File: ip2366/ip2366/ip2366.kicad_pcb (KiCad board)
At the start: 4 copper layers, 60 parts, among them CN1 XT30PW-M, Q1 RU3030M2-VB, SW1 K2-1112SW-A4SW-04, U1 IP2366 (I2C VERSION)

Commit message: replace the inductor
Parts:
- L1: footprint easyeda2kicad:IND-SMD_2P-L16.9-W16.9 -> easyeda2kicad:IND-SMD_L13.5-W12.5
- moved L1 2.54 mm to (146.9, 83.2)
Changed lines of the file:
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@@
 		)
 	)
-	(footprint "easyeda2kicad:IND-SMD_2P-L16.9-W16.9"
-		(layer "F.Cu")
-		(at 146.55 85.75)
-		(property "Reference" "L1"
-			(at 0 -4 0)
-			(layer "F.SilkS")
-			(effects
-				(font
-					(size 1 1)
-					(thickness 0.15)
-				)
-			)
-		)
-		(property "Value" "10uH"
-			(at 0 4 0)
-			(layer "F.Fab")
-			(effects
-				(font
-					(size 1 1)
-					(thickness 0.15)
-				)
-			)
-		)
-		(property "Datasheet" ""
-			(at 0 0 0)
-			(layer "F.Fab")
-			(hide yes)
-			(effects
-				(font
-					(size 1.27 1.27)
-					(thickness 0.15)
-				)
-			)
-		)
-		(property "Description" ""
-			(at 0 0 0)
-			(layer "F.Fab")
-			(hide yes)
-			(effects
-				(font
-					(size 1.27 1.27)
-					(thickness 0.15)
-				)
-			)
-		)
-		(property "LCSC Part" "C2847588"
-			(at 0 0 0)
-			(unlocked yes)
-			(layer "F.Fab")
-			(hide yes)
-			(effects
-				(font
-					(size 1 1)
-					(thickness 0.15)
-				)
-			)
-		)
-		(sheetname "/")
-		(sheetfile "ip2366.kicad_sch")
-		(attr smd)
-		(fp_line
-			(start -8.83 -8.74)
-			(end -8.81 -6.49)
-			(stroke
-				(width 0.25)
-				(type solid)
-			)
-			(layer "F.SilkS")
-		)
-		(fp_line
-			(start -8.82 6.48)
-			(end -8.82 9.01)
-			(stroke
-				(width 0.25)
-				(type solid)
-			)
-			(layer "F.SilkS")
-		)
-		(fp_line
-			(start -8.82 9.01)
-			(end 8.96 8.92)
-			(stroke
-				(width 0.25)
-				(type solid)
-			)
-			(layer "F.SilkS")
-		)
-		(fp_line
-			(start 8.82 -8.77)
-			(end -8.83 -8.74)
-			(stroke
-				(width 0.25)
-				(type solid)
-			)
-			(layer "F.SilkS")
-		)
-		(fp_line
-			(start 8.84 -6.49)
-			(end 8.82 -8.77)
-			(stroke
-				(width 0.25)
-				(type solid)
-			)
-			(layer "F.SilkS")
-		)
-		(fp_line
-			(start 8.96 8.92)
-			(end 8.94 6.48)
-			(stroke
-				(width 0.25)
-				(type solid)
-			)
-			(layer "F.SilkS")
-		)
-		(fp_circle
-			(center -8.8 -8.45)
-			(end -8.77 -8.45)
-			(stroke
-				(width 0.06)
-				(type solid)
-			)
-			(fill no)
-			(layer "F.Fab")
-		)
-		(fp_text user "${REFERENCE}"
-			(at 0 0 0)
-			(layer "F.Fab")
-			(effects
-				(font
-					(size 1 1)
-					(thickness 0.15)
-				)
-			)
-		)
-		(pad "1" smd rect
-			(at -7.7 0)
-			(size 3.15 12.5)
-			(layers "F.Cu" "F.Mask" "F.Paste")
-			(net 6 "LX1")
-			(pinfunction "1")
-			(pintype "unspecified")
-		)
-		(pad "2" smd rect
-			(at 7.7 0)
-			(size 3.15 12.5)
-			(layers "F.Cu" "F.Mask" "F.Paste")
-			(net 9 "LX2")
-			(pinfunction "2")
-			(pintype "unspecified")
-		)
-		(embedded_fonts no)
-		(model "${EASYEDA2KICAD}/easyeda2kicad.3dshapes/IND-SMD_2P-L16.9-W16.9.wrl"
-			(offset
-				(xyz 0 -0 -0)
-			)
-			(scale
-				(xyz 1 1 1)
-			)
-			(rotate
-				(xyz 0 0 0)
-			)
-		)
-	)
 	(footprint "easyeda2kicad:C1210"
 		(layer "F.Cu")
@@
 			)
 		)
+	)
+	(footprint "easyeda2kicad:IND-SMD_L13.5-W12.5"
+		(layer "F.Cu")
+		(at 146.86 83.225)
+		(property "Reference" "L1"
+			(at 0 -4 0)
+			(layer "F.SilkS")
+			(effects
+				(font
+					(size 1 1)
+					(thickness 0.15)
+				)
+			)
+		)
+		(property "Value" "10uH"
+			(at 0 4 0)
+			(layer "F.Fab")
+			(effects
+				(font
+					(size 1 1)
+					(thickness 0.15)
+				)
+			)
+		)
+		(property "Datasheet" ""
+			(at 0 0 0)
+			(layer "F.Fab")
+			(hide yes)
+			(effects
+				(font
+					(size 1.27 1.27)
+					(thickness 0.15)
+				)
+			)
+		)
+		(property "Description" ""
+			(at 0 0 0)
+			(layer "F.Fab")
+			(hide yes)
+			(effects
+				(font
+					(size 1.27 1.27)
+					(thickness 0.15)
+				)
+			)
+		)
+		(property "LCSC Part" "C840531"
+			(at 0 0 0)
+			(unlocked yes)
+			(layer "F.Fab")
+			(hide yes)
+			(effects
+				(font
+					(size 1 1)
+					(thickness 0.15)
+				)
+			)
+		)
+		(sheetname "/")
+		(sheetfile "ip2366.kicad_sch")
+		(attr through_hole)
+		(fp_line
+			(start -6.86 -6.35)
+			(end 6.86 -6.35)
+			(stroke
+				(width 0.25)
+				(type solid)
+			)
+			(layer "F.SilkS")
+		)
+		(fp_line
+			(start -6.86 -2.98)
+			(end -6.86 -6.35)
+			(stroke
+				(width 0.25)
+				(type solid)
+			)
+			(layer "F.SilkS")
+		)
+		(fp_line
+			(start -6.86 6.35)
+			(end -6.86 3.05)
+			(stroke
+				(width 0.25)
+				(type solid)
+			)
+			(layer "F.SilkS")
+		)
+		(fp_line
+			(start 6.86 -6.35)
+			(end 6.86 -3.05)
+			(stroke
+				(width 0.25)
+				(type solid)
+			)
+			(layer "F.SilkS")
+		)
+		(fp_line
+			(start 6.86 2.98)
+			(end 6.86 6.35)
+			(stroke
+				(width 0.25)
+				(type solid)
+			)
+			(layer "F.SilkS")
+		)
+		(fp_line
+			(start 6.86 6.35)
+			(end -6.86 6.35)
+			(stroke
+				(width 0.25)
+				(type solid)
+			)
+			(layer "F.SilkS")
+		)
+		(fp_circle
+			(center -6.75 6.25)
+			(end -6.72 6.25)
+			(stroke
+				(width 0.06)
+				(type solid)
+			)
+			(fill no)
+			(layer "F.Fab")
+		)
+		(fp_text user "${REFERENCE}"
+			(at 0 0 0)
+			(layer "F.Fab")
+			(effects
+				(font
+					(size 1 1)
+					(thickness 0.15)
+				)
+			)
+		)
+		(pad "1" smd rect
+			(at -5.39 0)
+			(size 4.18 5.5)
+			(layers "F.Cu" "F.Mask" "F.Paste")
+			(net 6 "LX1")
+			(pinfunction "1")
+			(pintype "unspecified")
+		)
+		(pad "2" smd rect
+			(at 5.39 0)
+			(size 4.18 5.5)
+			(layers "F.Cu" "F.Mask" "F.Paste")
+			(net 9 "LX2")
+			(pinfunction "2")
+			(pintype "unspecified")
+		)
+		(embedded_fonts no)
+		(model "${EASYEDA2KICAD}/easyeda2kicad.3dshapes/IND-SMD_L13.5-W12.5.wrl"
+			(offset
+				(xyz 0 -0 0)
+			)
+			(scale
+				(xyz 1 1 1)
+			)
+			(rotate
+				(xyz 0 0 0)
+			)
+		)

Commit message: aktueller stand
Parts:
- added R21: 0R, Resistor_SMD:R_0603_1608Metric_Pad0.98x0.95mm_HandSolder, F.Cu at (146.3, 52.4)
- moved C22 48.1 mm to (159.6, 52.9)
- moved C23 47.6 mm to (165.4, 53.3)
- moved C20 47.4 mm to (156.2, 52.9)
- moved C19 46.7 mm to (152.8, 52.9)
- moved C2 45.4 mm to (119.5, 52.8)
- moved Q1 45.4 mm to (114.5, 59.2)
- moved C4 44.8 mm to (122.9, 52.8)
- moved C6 44.2 mm to (126.2, 52.8)
- moved R3 43.1 mm to (117.9, 60.7), turned to 180 degrees
- moved CN1 42.1 mm to (173.1, 63.0)
- moved C5 40.5 mm to (115.2, 64.8)
- moved SW1 39.8 mm to (101.7, 74.3)
- moved R20 39.4 mm to (105.6, 73.9), turned to 180 degrees
- moved R19 38.7 mm to (105.6, 72.3), turned to 180 degrees
- moved C7 38.5 mm to (109.8, 57.0), turned to 180 degrees
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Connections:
- Q1 pad 1: unconnected-(Q1-S-Pad1) -> VBUS
- Q1 pad 3: unconnected-(Q1-S-Pad3) -> VBUS
- RNTC1 pad 1: NTC -> Net-(R21-Pad2)
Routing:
- net +BATT: track 0.00 -> 126.0 mm, vias 0 -> 1
- net EN: track 0.00 -> 74.5 mm, vias 0 -> 2
- net CC2: track 0.00 -> 59.2 mm, vias 0 -> 2
- net DP: track 0.00 -> 58.0 mm, vias 0 -> 2
- net DM: track 0.00 -> 56.4 mm, vias 0 -> 2
- net CC1: track 0.00 -> 50.4 mm, vias 0 -> 2
- net VBUS: track 0.00 -> 38.4 mm, vias 0 -> 2
- net LED3: track 0.00 -> 37.8 mm, vias 0 -> 2
- net VBUS1: track 0.00 -> 37.5 mm
- net LED2: track 0.00 -> 37.2 mm, vias 0 -> 2
- net LED1: track 0.00 -> 35.9 mm, vias 0 -> 2
- net VSET: track 0.00 -> 29.1 mm, vias 0 -> 2
- net LG1: track 0.00 -> 27.3 mm, vias 0 -> 2
- net LG2: track 0.00 -> 27.2 mm, vias 0 -> 2
- net PSET: track 0.00 -> 25.9 mm, vias 0 -> 4
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- added copper zone on F.Cu, net +BATT
- added copper zone on F.Cu, net -BATT
- added copper zone on B.Cu, net GND
- added copper zone on F.Cu, net GND
- added copper zone on In1.Cu, net GND
- added copper zone on In2.Cu, net GND
- added copper zone on F.Cu, net LX1
- added copper zone on F.Cu, net LX2
- added copper zone on F.Cu, net VBUS
- added copper zone on F.Cu, net VBUS-
- added copper zone on F.Cu, net VBUS1
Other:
- board outline added: 80 x 32 mm
- board text added: "+"

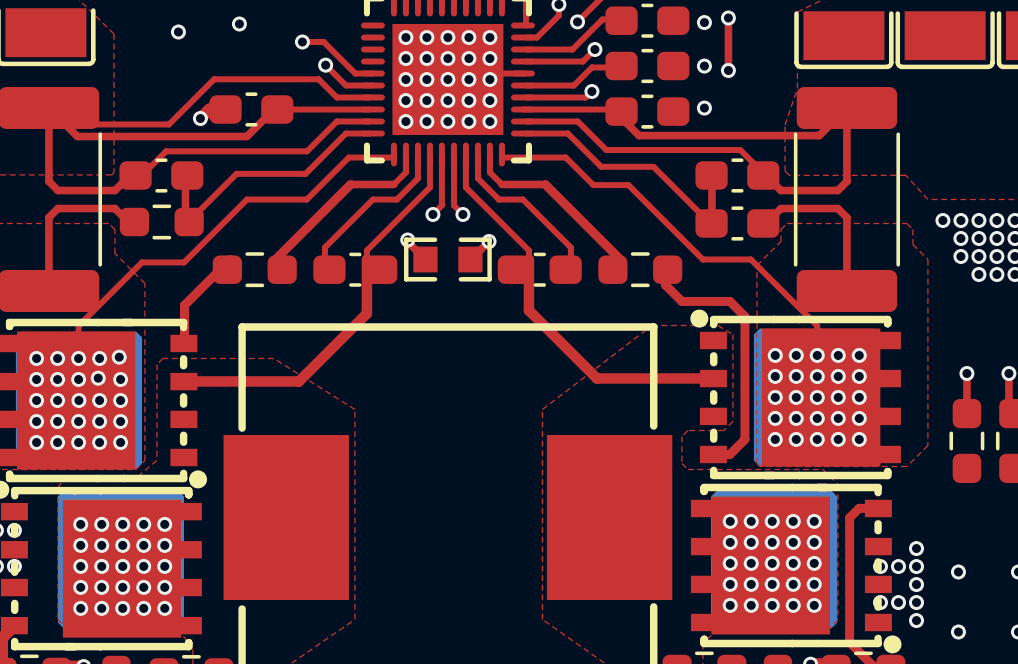
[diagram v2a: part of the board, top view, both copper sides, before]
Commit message: add teardrops
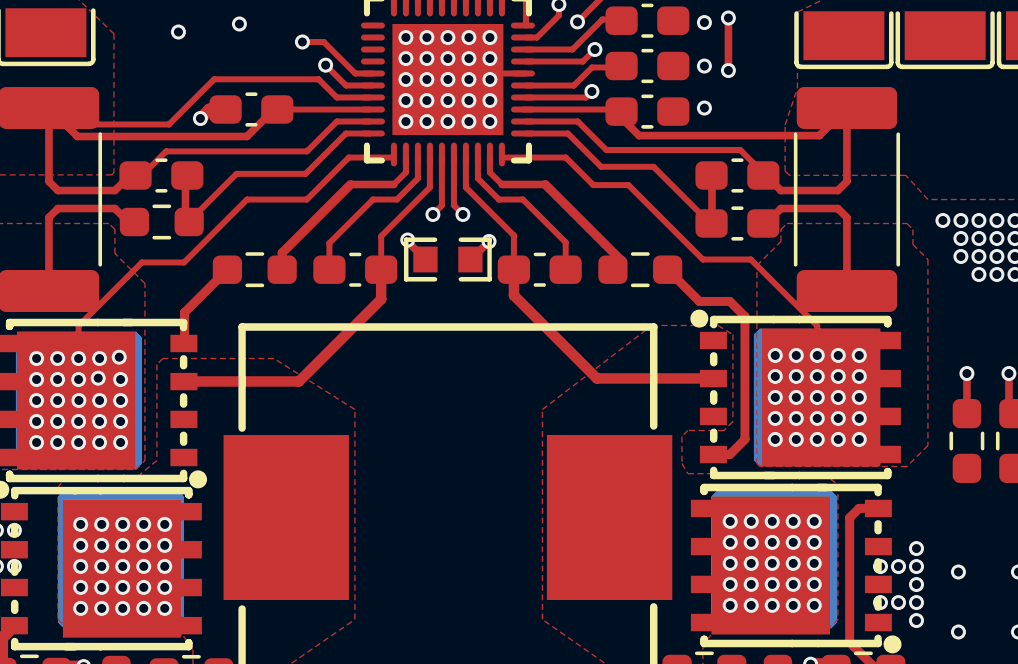
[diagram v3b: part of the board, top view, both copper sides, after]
